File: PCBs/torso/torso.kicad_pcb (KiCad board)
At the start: 2 copper layers, 140 x 81 mm, 5 parts

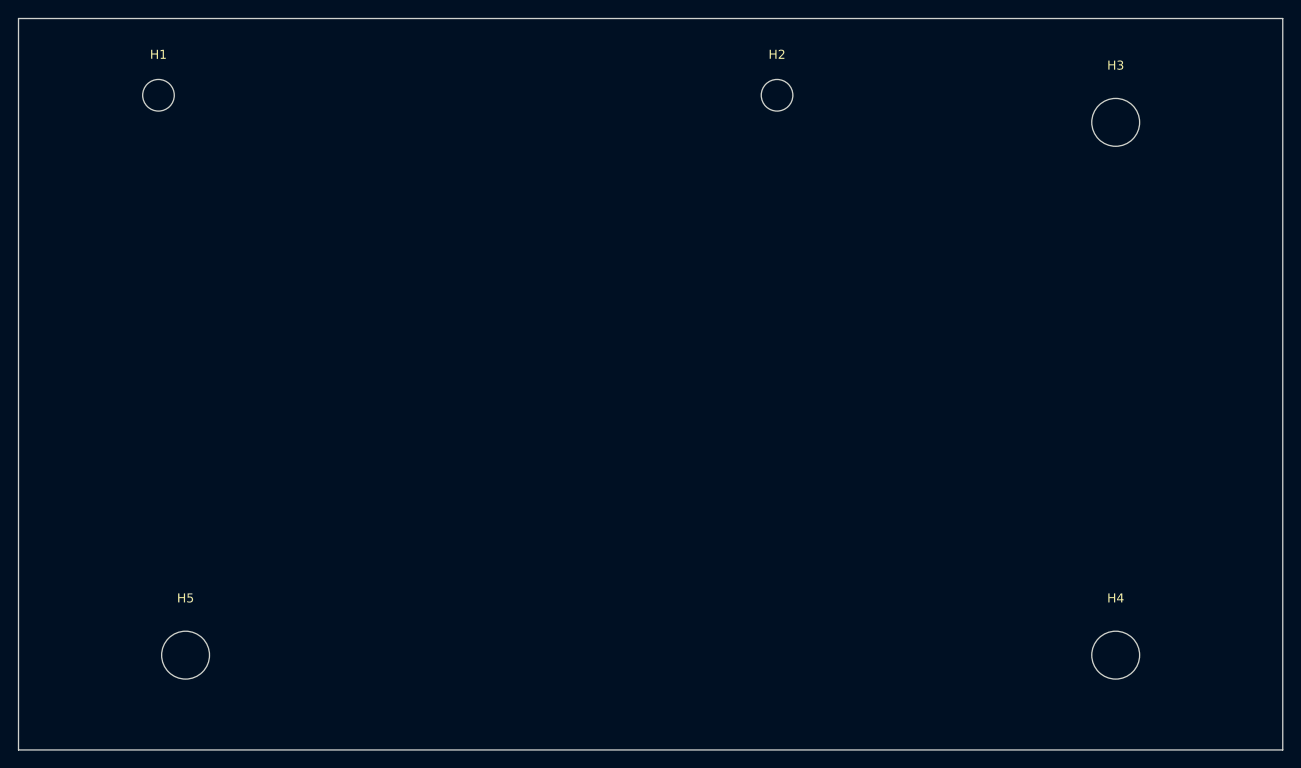
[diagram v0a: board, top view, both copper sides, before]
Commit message: Torso all but complete, making bogie before checking the last mark
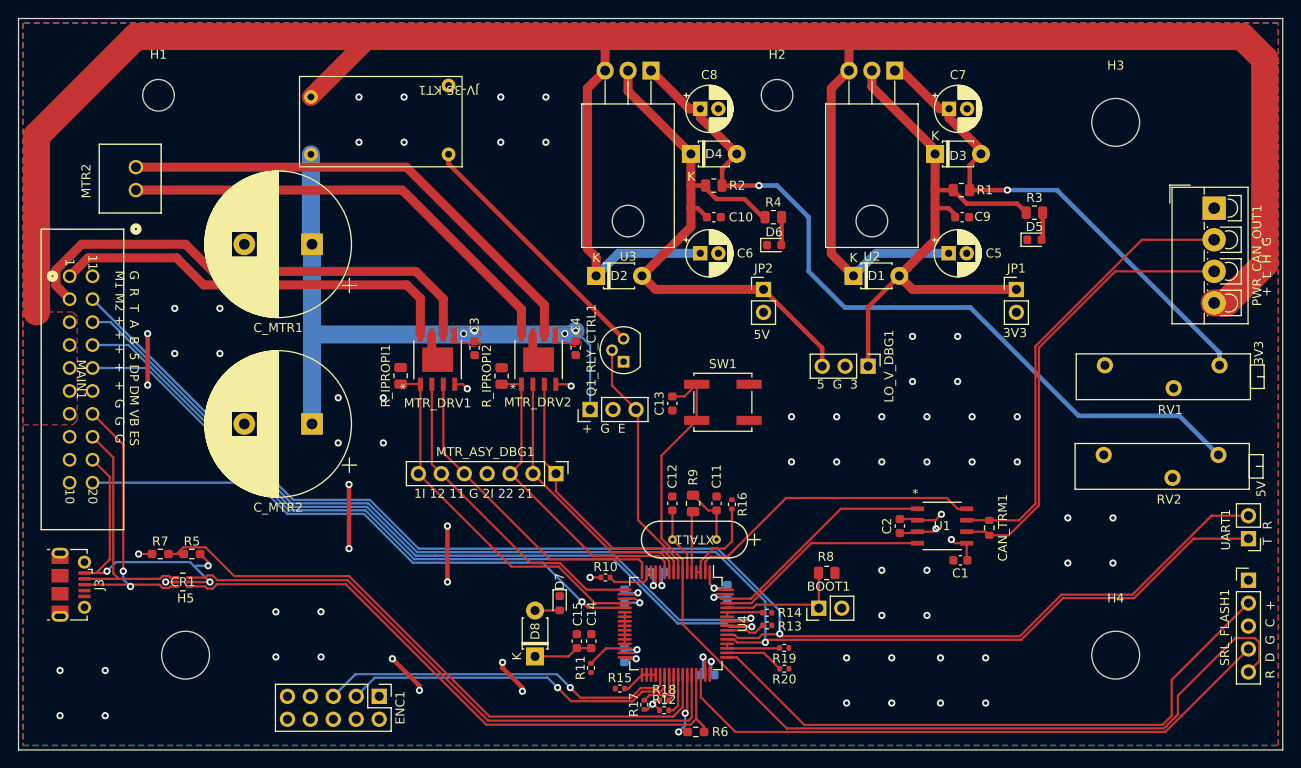
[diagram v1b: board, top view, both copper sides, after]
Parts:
- added BOOT1: BOOTMODE, Connector_PinHeader_2.54mm:PinHeader_1x02_P2.54mm_Vertical, F.Cu at (118.6, 85.3)
- added C1: 100nF, Capacitor_SMD:C_0603_1608Metric, F.Cu at (134.3, 80.0)
- added C10: 100nF, Capacitor_SMD:C_0603_1608Metric, F.Cu at (107.0, 42.0)
- added C11: 20pF, Capacitor_SMD:C_0603_1608Metric, F.Cu at (107.3, 73.7)
- added C12: 20pF, Capacitor_SMD:C_0603_1608Metric, F.Cu at (102.4, 73.7)
- added C13: 100nF, Capacitor_SMD:C_0603_1608Metric, F.Cu at (102.4, 62.6)
- added C14: 4.7muF, Capacitor_SMD:C_0603_1608Metric, F.Cu at (93.4, 88.9)
- added C15: 1muF, Capacitor_SMD:C_0603_1608Metric, F.Cu at (91.8, 88.9)
- added C16: 10nF, Capacitor_SMD:C_0603_1608Metric, B.Cu at (100.8, 81.3)
- added C17: 100nF, Capacitor_SMD:C_0603_1608Metric, B.Cu at (108.5, 83.5)
- added C18: 100nF, Capacitor_SMD:C_0603_1608Metric, B.Cu at (106.3, 92.7)
- added C19: 100nF, Capacitor_SMD:C_0603_1608Metric, B.Cu at (97.1, 90.5)
- added C2: 100nF, Capacitor_SMD:C_0603_1608Metric, F.Cu at (127.6, 76.2)
- added C20: 100nF, Capacitor_SMD:C_0603_1608Metric, B.Cu at (97.1, 84.0)
- added C3: 100nF, Capacitor_SMD:C_0603_1608Metric, F.Cu at (80.5, 56.5)
- added C4: 100nF, Capacitor_SMD:C_0603_1608Metric, F.Cu at (91.7, 56.5)
- added C5: 10muF, Capacitor_THT:CP_Radial_D5.0mm_P2.00mm, F.Cu at (133.0, 46.0)
- added C6: 10muF, Capacitor_THT:CP_Radial_D5.0mm_P2.00mm, F.Cu at (105.5, 46.0)
- added C7: 10muF, Capacitor_THT:CP_Radial_D5.0mm_P2.00mm, F.Cu at (133.0, 30.0)
- added C8: 10muF, Capacitor_THT:CP_Radial_D5.0mm_P2.00mm, F.Cu at (105.5, 30.0)
- added C9: 100nF, Capacitor_SMD:C_0603_1608Metric, F.Cu at (134.5, 42.0)
- added CAN_TRM1: 120Ohm, Resistor_SMD:R_0603_1608Metric, F.Cu at (137.5, 76.4)
- added CR1: USBLC6-2P6, USBLC6:SOT-666_STM, F.Cu at (48.2, 82.4)
- added C_MTR1: 330uF, Capacitor_THT:CP_Radial_D16.0mm_P7.50mm, F.Cu at (62.5, 45.0)
- added C_MTR2: 330uF, Capacitor_THT:CP_Radial_D16.0mm_P7.50mm, F.Cu at (62.5, 64.9)
- added D1: IN4005, Diode_THT:D_T-1_P5.08mm_Horizontal, F.Cu at (122.5, 48.5)
- added D2: IN4005, Diode_THT:D_T-1_P5.08mm_Horizontal, F.Cu at (94.0, 48.5)
- added D3: IN4005, Diode_THT:D_T-1_P5.08mm_Horizontal, F.Cu at (131.5, 35.0)
- added D4: IN4005, Diode_THT:D_T-1_P5.08mm_Horizontal, F.Cu at (104.5, 35.0)
- added D5: LED_3V3, LED_SMD:LED_0603_1608Metric, F.Cu at (142.5, 44.5)
- added D6: LED_5V, LED_SMD:LED_0603_1608Metric, F.Cu at (113.7, 45.1)
- added D7: LED, LED_SMD:LED_0603_1608Metric, F.Cu at (89.9, 84.7)
- added D8: D_Zener, Diode_THT:D_T-1_P5.08mm_Horizontal, F.Cu at (87.2, 90.6)
- added ENC1: Conn_02x05_Odd_Even, Connector_PinHeader_2.54mm:PinHeader_2x05_P2.54mm_Vertical, F.Cu at (69.9, 95.1)
- added J3: USB_B_Micro, Connector_USB:USB_Micro-B_Molex-105017-0001, F.Cu at (35.8, 82.7)
- added JP1: Jumper_2_Open, Connector_PinHeader_2.54mm:PinHeader_1x02_P2.54mm_Vertical, F.Cu at (140.5, 50.0)
- added JP2: Jumper_2_Open, Connector_PinHeader_2.54mm:PinHeader_1x02_P2.54mm_Vertical, F.Cu at (112.5, 50.0)
- added JV-3S-KT1: RELAY, JV-3S-KT:JV-3S-KT, F.Cu at (70.0, 32.5)
- added LO_V_DBG1: Conn_01x03, Connector_PinHeader_2.54mm:PinHeader_1x03_P2.54mm_Vertical, F.Cu at (124.1, 58.5)
- added MAIN1: Conn_02x10_Top_Bottom, 1761681-7:1761681-7_TYC, F.Cu at (35.7, 48.5)
- added MTR2: 705430001, 70543-0001:70543-0001_MOL, F.Cu at (43.0, 39.0)
- added MTR_ASY_DBG1: Conn_01x07, Connector_PinHeader_2.54mm:PinHeader_1x07_P2.54mm_Vertical, F.Cu at (89.5, 70.4)
- added MTR_DRV1: DRV8251ADDAR, DRV8251A:SOIC8_DDA_TEX, F.Cu at (76.4, 57.8)
- added MTR_DRV2: DRV8251ADDAR, DRV8251A:SOIC8_DDA_TEX, F.Cu at (87.6, 57.8)
- added PWR_CAN_OUT1: Conn_01x04, TerminalBlock_4Ucon:TerminalBlock_4Ucon_1x04_P3.50mm_Vertical, F.Cu at (162.4, 41.0)
- added Q1_RLY_CTRL1: Q_NIGBT_CGE, Package_TO_SOT_THT:TO-92, F.Cu at (97.0, 58.0)
- added R1: 240Ohm, Resistor_SMD:R_0805_2012Metric, F.Cu at (134.4, 39.0)
- added R10: 40kOhm, Resistor_SMD:R_0402_1005Metric, F.Cu at (95.0, 81.9)
- added R11: 40kOhm, Resistor_SMD:R_0402_1005Metric, F.Cu at (93.4, 91.9)
- added R12: 40kOhm, Resistor_SMD:R_0402_1005Metric, F.Cu at (101.5, 96.6)
- added R13: 40kOhm, Resistor_SMD:R_0402_1005Metric, F.Cu at (112.9, 87.2)
- added R14: 40kOhm, Resistor_SMD:R_0402_1005Metric, F.Cu at (112.9, 85.8)
- added R15: 40kOhm, Resistor_SMD:R_0402_1005Metric, F.Cu at (96.6, 94.2)
- added R16: 40kOhm, Resistor_SMD:R_0402_1005Metric, F.Cu at (109.0, 73.8)
- added R17: 40kOhm, Resistor_SMD:R_0402_1005Metric, F.Cu at (99.3, 96.0)
- added R18: 40kOhm, Resistor_SMD:R_0402_1005Metric, F.Cu at (101.5, 95.5)
- added R19: 40kOhm, Resistor_SMD:R_0402_1005Metric, F.Cu at (114.8, 89.7)
- added R2: 240Ohm, Resistor_SMD:R_0805_2012Metric, F.Cu at (107.0, 38.5)
- added R20: 40kOhm, Resistor_SMD:R_0402_1005Metric, F.Cu at (114.8, 92.0)
- added R3: 1k5, Resistor_SMD:R_0805_2012Metric, F.Cu at (142.5, 41.5)
- added R4: 1k5, Resistor_SMD:R_0805_2012Metric, F.Cu at (113.6, 42.0)
- added R5: 82k, Resistor_SMD:R_0603_1608Metric_Pad0.98x0.95mm_HandSolder, F.Cu at (49.2, 79.3)
- added R6: 1k5, Resistor_SMD:R_0603_1608Metric_Pad0.98x0.95mm_HandSolder, F.Cu at (105.0, 99.0)
- added R7: 33k, Resistor_SMD:R_0603_1608Metric_Pad0.98x0.95mm_HandSolder, F.Cu at (45.7, 79.3)
- added R8: 10kOhm, Resistor_SMD:R_0805_2012Metric, F.Cu at (119.5, 81.4)
- added R9: 340Ohm, Resistor_SMD:R_0805_2012Metric, F.Cu at (104.7, 73.7)
- added RLY_CTL_DBG1: Conn_01x03, Connector_PinHeader_2.54mm:PinHeader_1x03_P2.54mm_Vertical, F.Cu at (93.3, 63.3)
- added RV1: 0,386k, Potentiometer_THT:Potentiometer_Bourns_3006P_Horizontal, F.Cu at (150.3, 58.4)
- added RV2: 0,706k, Potentiometer_THT:Potentiometer_Bourns_3006P_Horizontal, F.Cu at (150.2, 68.3)
- added R_IPROPI1: 510Ohm, Resistor_SMD:R_0805_2012Metric, F.Cu at (72.3, 59.6)
- added R_IPROPI2: 510Ohm, Resistor_SMD:R_0805_2012Metric, F.Cu at (83.5, 59.6)
- added SRL_FLASH1: Conn_01x05, Connector_PinHeader_2.54mm:PinHeader_1x05_P2.54mm_Vertical, F.Cu at (166.2, 82.2)
- added SW1: RESET, Button_Switch_SMD:SW_Push_1P1T_NO_CK_KSC6xxJ, F.Cu at (108.0, 62.5)
- added U1: TJA1057GT/3J, TJA1057BT:SOT96-1_SO8_NXP, F.Cu at (132.3, 76.2)
- added U2: LM317_TO-220, Package_TO_SOT_THT:TO-220-3_Horizontal_TabDown, F.Cu at (127.0, 25.8)
- added U3: LM317_TO-220, Package_TO_SOT_THT:TO-220-3_Horizontal_TabDown, F.Cu at (100.0, 25.8)
- added U4: STM32F303RETx, Package_QFP:LQFP-64_10x10mm_P0.5mm, F.Cu at (102.8, 87.0)
- added UART1: Conn_01x02, Connector_PinHeader_2.54mm:PinHeader_1x02_P2.54mm_Vertical, F.Cu at (166.2, 77.6)
- added XTAL1: ABL-16.000MHZ-B2, ABL-16.000MHZ-B1U-T:XTAL_ABL-16_ABR, F.Cu at (107.3, 77.7)
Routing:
- net +48V: track 0.00 -> 281.4 mm
- net /UART_RX: track 0.00 -> 156.6 mm, vias 0 -> 1
- net /UART_TX: track 0.00 -> 154.5 mm, vias 0 -> 1
- net /RESET: track 0.00 -> 110.4 mm
- net Net-(D4-A): track 0.00 -> 88.9 mm, vias 0 -> 1
- net /ENC1B: track 0.00 -> 88.3 mm, vias 0 -> 1
- net /ENC1A: track 0.00 -> 87.6 mm, vias 0 -> 1
- net /USB_DP: track 0.00 -> 69.8 mm
- net /USB_VBUS: track 0.00 -> 69.8 mm
- net Net-(JV-3S-KT1-COM): track 0.00 -> 69.6 mm, vias 0 -> 4
- net /FLASH_CLK: track 0.00 -> 68.7 mm
- net /FLASH_DIO: track 0.00 -> 68.5 mm
- net /USB_DM: track 0.00 -> 67.3 mm
- net Net-(D1-A): track 0.00 -> 66.2 mm
- net Net-(D2-A): track 0.00 -> 65.1 mm
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- added copper zone on In2.Cu, net +3V3
- added copper zone on F.Cu, net +48V
- added copper zone on B.Cu, net +5V
- added copper zone on F.Cu, net GND
- added copper zone on In1.Cu, net GND
- added copper zone on F.Cu, net Net-(JV-3S-KT1-COM)
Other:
- copper layers 2 -> 4
- board text added: "+ G E"
- board text added: "+ L H G"
- board text added: "1I 12 11 G 2I 22 21"
- board text added: "3V3"
- board text added: "5 G 3"
- board text added: "5V"
- board text added: "G R T A B 5 DP DM VB ES M1 M2 + + + + + G G G"
- board text added: "R D G C +"
- board text added: "T R"

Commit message: Torso, bogie and rail complete. Next up: revise hand and IMU board in conjunction
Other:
- board text added: "KRISTIAN BLOM"
- board text added: "TTK4900 TORSO MK1.1"

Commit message: All revisions finished, MK1.1 ready for gerber generation
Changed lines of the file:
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@@
     (property "ki_keywords" "connector")
     (attr through_hole)
-    (fp_text reference "PWR_CAN_OUT1" (at 5.25 -4.76 90) (layer "F.SilkS")
+    (fp_text reference "PWR_CAN_OUT1" (at 5.7 6.5 90) (layer "F.SilkS")
         (effects (font (size 1 1) (thickness 0.15)))
     )
@@
     (effects (font (size 1 1) (thickness 0.1875)) (justify left bottom))
   )
-  (gr_text "+  L  H  G" (at 168.8 50.8 90) (layer "F.SilkS")
+  (gr_text "+   L   H   G" (at 168.3 51.5 90) (layer "F.SilkS")
     (effects (font (size 1 1) (thickness 0.1875)) (justify left bottom))
   )
